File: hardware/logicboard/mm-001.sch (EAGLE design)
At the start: 25 parts, among them IC1 74ALS05N, IC2 LTC485N, IC3 LTC485N

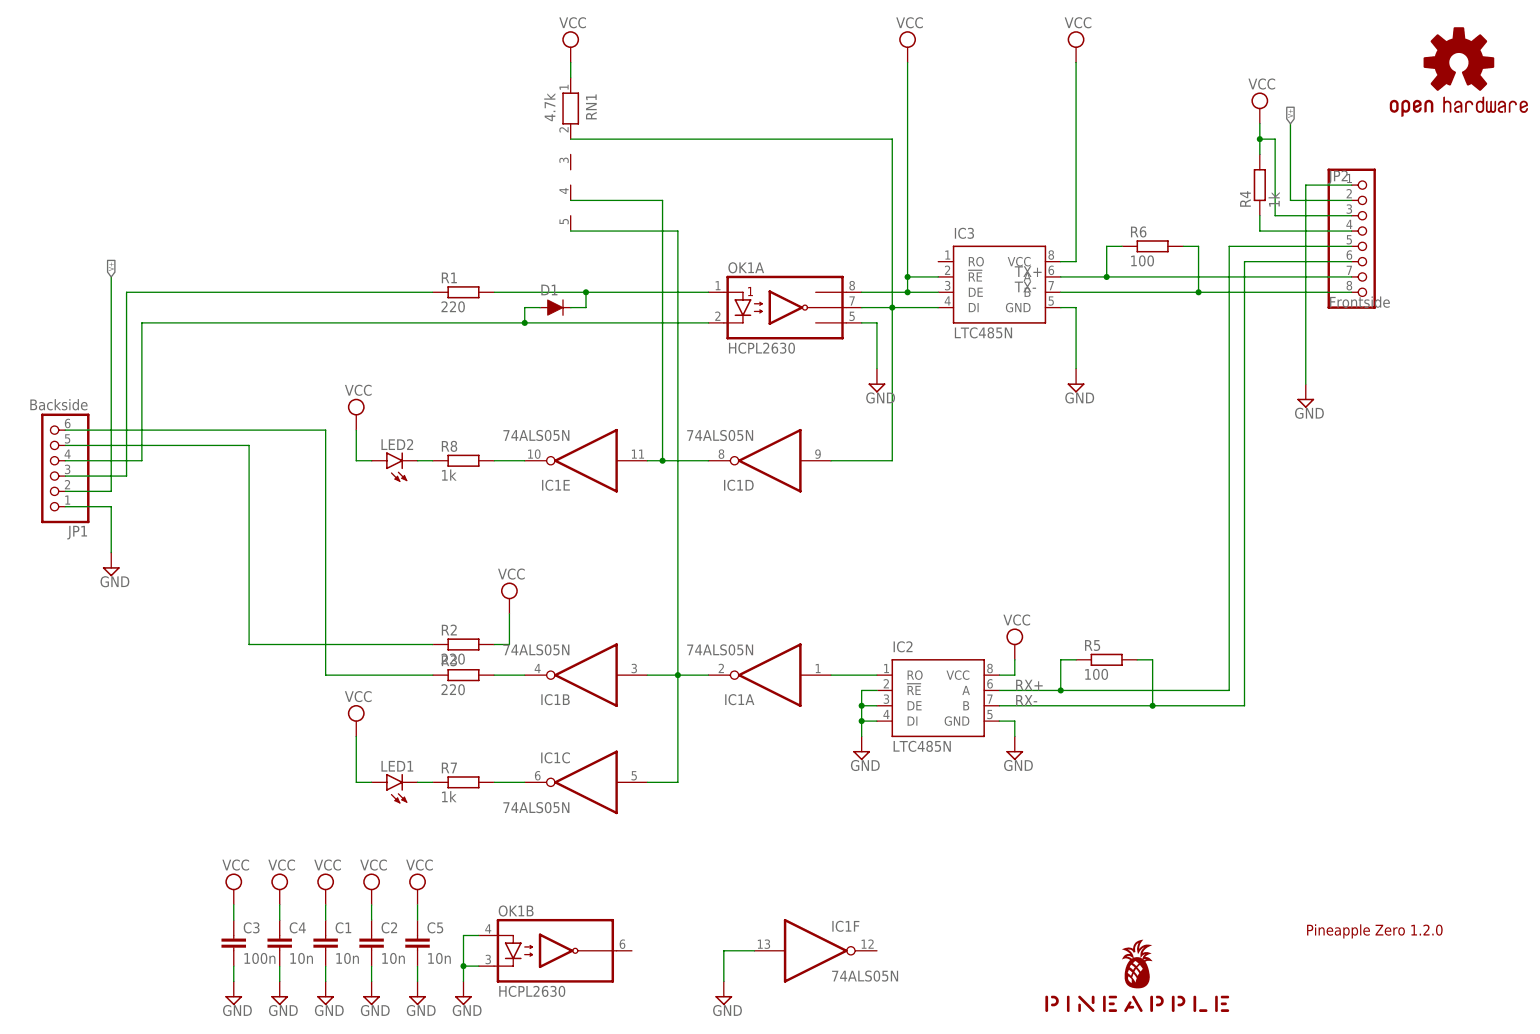
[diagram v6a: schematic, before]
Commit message: TX+/TX-/GND, RX+/RX-/GND.
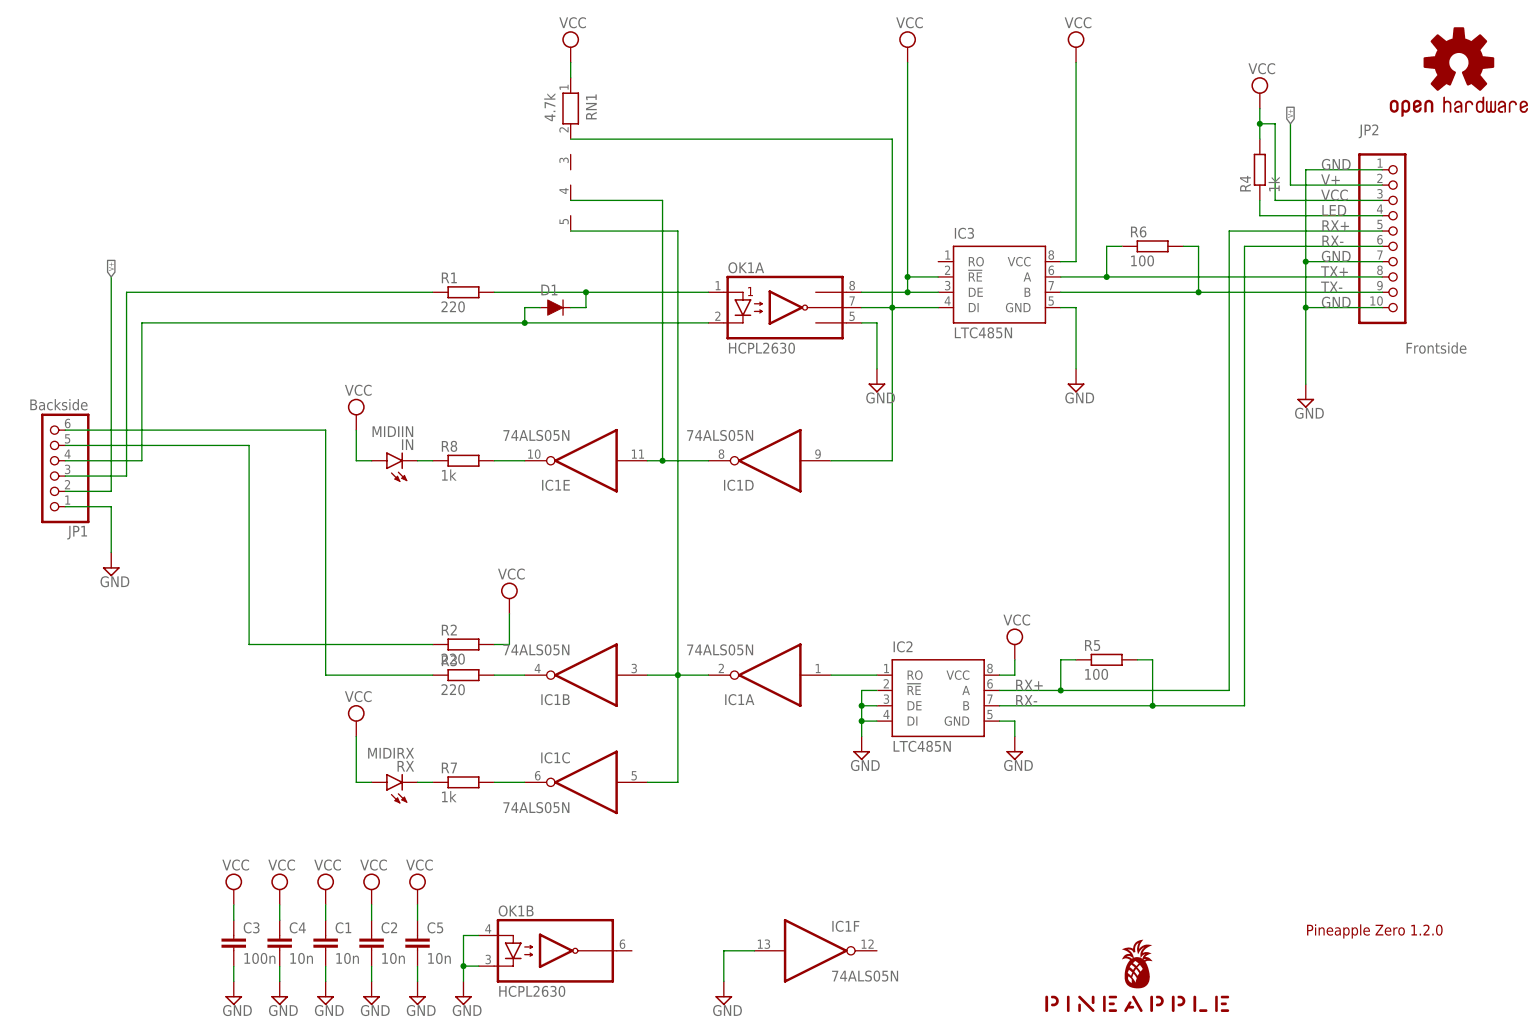
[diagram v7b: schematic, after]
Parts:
- IN: value (none) -> MIDIIN
- JP2: device pinhead:PINHD-1X8 -> pinhead:PINHD-1X10
- RX: value (none) -> MIDIRX
- renumbered LED1 to RX, LED2 to IN
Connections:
- net GND: now also JP2.10, JP2.7
- net TX+: now also JP2.8; no longer JP2.7
- net TX-: now also JP2.9; no longer JP2.8
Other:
- moved on the sheet: R4

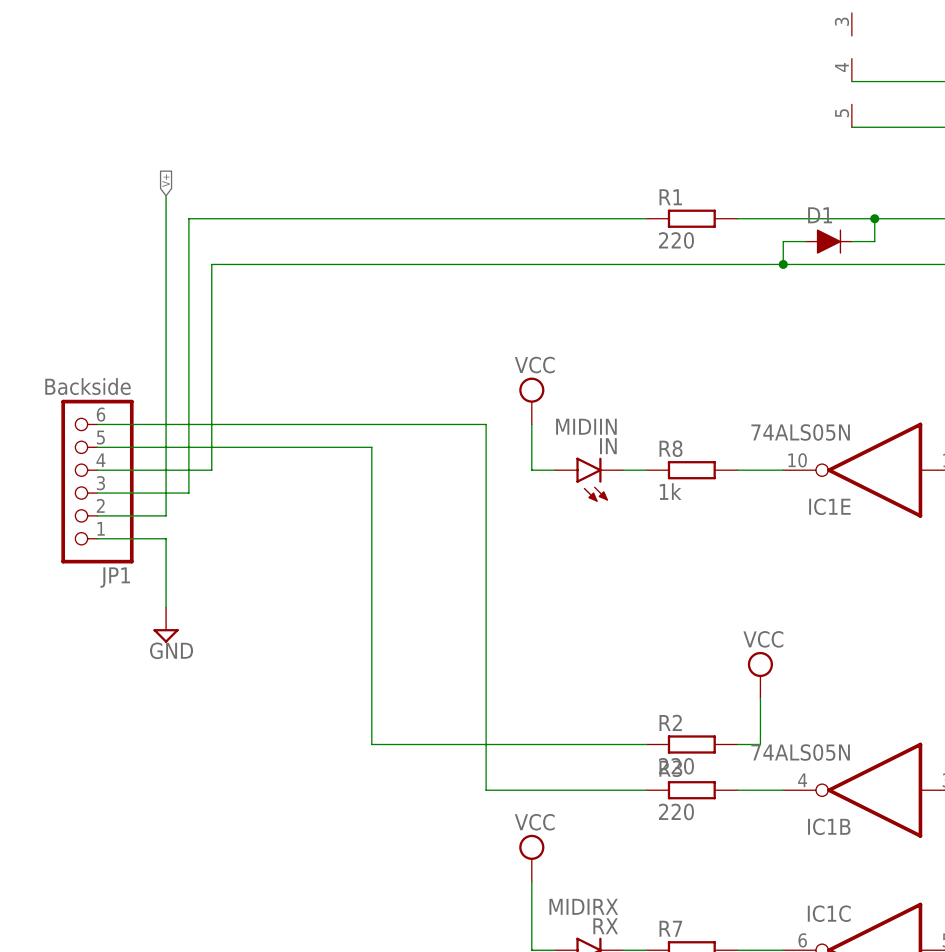
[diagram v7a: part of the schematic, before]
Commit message: Changed positions of the monitor leds.
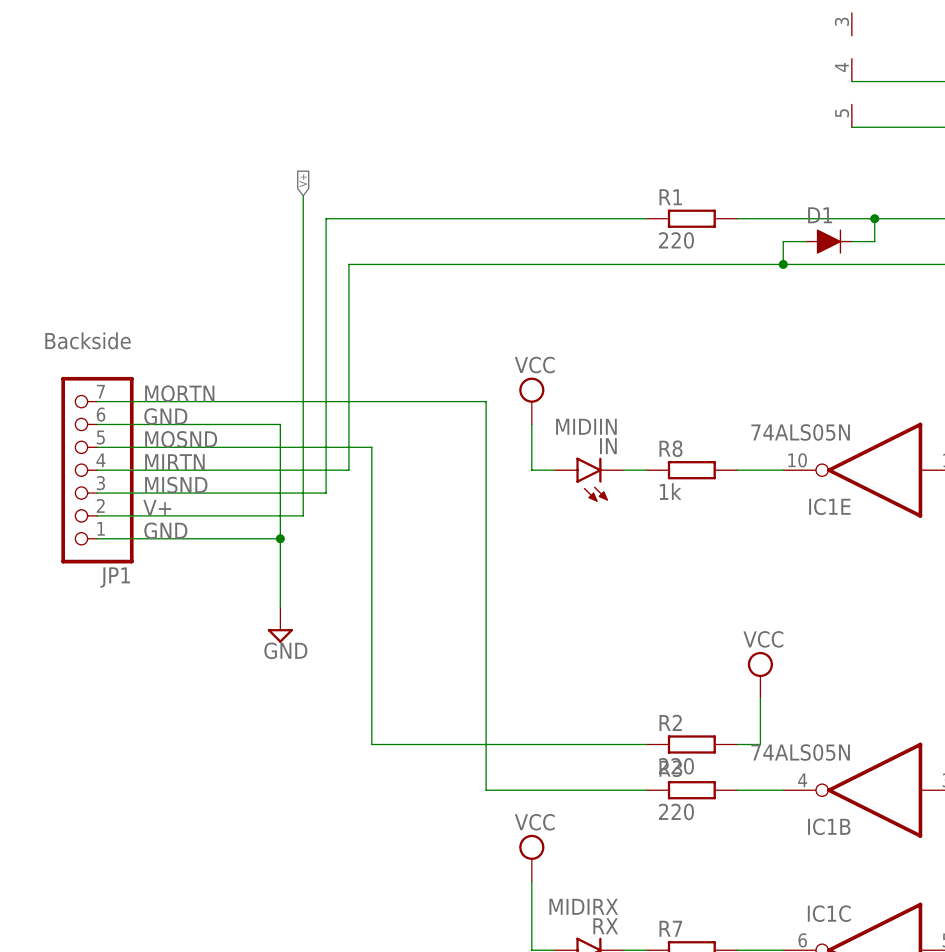
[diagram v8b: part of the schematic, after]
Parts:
- IN, RX: device led:LED3MM -> led:LEDB152
- JP1: device pinhead:PINHD-1X6 -> pinhead:PINHD-1X7
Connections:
- net GND: now also JP1.6
- net MORTN: now also JP1.7; no longer JP1.6
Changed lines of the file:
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@@
 <part name="SUPPLY22" library="supply2" library_urn="urn:adsk.eagle:library:372" deviceset="GND" device=""/>
 <part name="SUPPLY25" library="supply2" library_urn="urn:adsk.eagle:library:372" deviceset="GND" device=""/>
-<part name="JP1" library="pinhead" library_urn="urn:adsk.eagle:library:325" deviceset="PINHD-1X6" device="" package3d_urn="urn:adsk.eagle:package:22472/2" value="Backside"/>
+<part name="JP1" library="pinhead" library_urn="urn:adsk.eagle:library:325" deviceset="PINHD-1X7" device="" package3d_urn="urn:adsk.eagle:package:22477/2" value="Backside"/>
 <part name="JP2" library="pinhead" library_urn="urn:adsk.eagle:library:325" deviceset="PINHD-1X10" device="" package3d_urn="urn:adsk.eagle:package:22406/2" value="Frontside"/>
 <part name="R6" library="rcl" library_urn="urn:adsk.eagle:library:334" deviceset="R-EU_" device="0204/5" package3d_urn="urn:adsk.eagle:package:23488/1" value="100"/>
 <part name="R7" library="rcl" library_urn="urn:adsk.eagle:library:334" deviceset="R-EU_" device="0204/5" package3d_urn="urn:adsk.eagle:package:23488/1" value="1k"/>
-<part name="RX" library="led" library_urn="urn:adsk.eagle:library:259" deviceset="LED" device="3MM" package3d_urn="urn:adsk.eagle:package:15797/1" value="MIDIRX"/>
+<part name="RX" library="led" library_urn="urn:adsk.eagle:library:259" deviceset="LED" device="B152" package3d_urn="urn:adsk.eagle:package:15803/1" value="MIDIRX"/>
 <part name="SUPPLY1" library="supply2" library_urn="urn:adsk.eagle:library:372" deviceset="VCC" device=""/>
 <part name="R8" library="rcl" library_urn="urn:adsk.eagle:library:334" deviceset="R-EU_" device="0204/5" package3d_urn="urn:adsk.eagle:package:23488/1" value="1k"/>
-<part name="IN" library="led" library_urn="urn:adsk.eagle:library:259" deviceset="LED" device="3MM" package3d_urn="urn:adsk.eagle:package:15797/1" value="MIDIIN"/>
+<part name="IN" library="led" library_urn="urn:adsk.eagle:library:259" deviceset="LED" device="B152" package3d_urn="urn:adsk.eagle:package:15803/1" value="MIDIIN"/>
 <part name="SUPPLY6" library="supply2" library_urn="urn:adsk.eagle:library:372" deviceset="VCC" device=""/>
 <part name="SUPPLY19" library="supply2" library_urn="urn:adsk.eagle:library:372" deviceset="GND" device=""/>
@@
 <attribute name="VALUE" x="72.39" y="60.198" size="1.778" layer="96"/>
 </instance>
-<instance part="SUPPLY22" gate="GND" x="17.78" y="81.28" smashed="yes">
-<attribute name="VALUE" x="15.875" y="78.105" size="1.778" layer="96"/>
+<instance part="SUPPLY22" gate="GND" x="30.48" y="81.28" smashed="yes">
+<attribute name="VALUE" x="28.575" y="78.105" size="1.778" layer="96"/>
 </instance>
 <instance part="SUPPLY25" gate="GND" x="215.9" y="109.22" smashed="yes">
@@
 <instance part="JP1" gate="A" x="7.62" y="99.06" smashed="yes" rot="R180">
 <attribute name="NAME" x="13.97" y="88.265" size="1.778" layer="95" rot="R180"/>
-<attribute name="VALUE" x="13.97" y="109.22" size="1.778" layer="96" rot="R180"/>
+<attribute name="VALUE" x="13.97" y="114.3" size="1.778" layer="96" rot="R180"/>
 </instance>
 <instance part="JP2" gate="A" x="231.14" y="137.16" smashed="yes">
@@
 </segment>
 <segment>
-<wire x1="10.16" y1="91.44" x2="17.78" y2="91.44" width="0.1524" layer="91"/>
-<wire x1="17.78" y1="91.44" x2="17.78" y2="83.82" width="0.1524" layer="91"/>
+<wire x1="10.16" y1="91.44" x2="30.48" y2="91.44" width="0.1524" layer="91"/>
+<wire x1="30.48" y1="91.44" x2="30.48" y2="83.82" width="0.1524" layer="91"/>
 <pinref part="SUPPLY22" gate="GND" pin="GND"/>
 <pinref part="JP1" gate="A" pin="1"/>
+<label x="15.24" y="91.44" size="1.778" layer="95"/>
+<pinref part="JP1" gate="A" pin="6"/>
+<wire x1="10.16" y1="104.14" x2="30.48" y2="104.14" width="0.1524" layer="91"/>
+<wire x1="30.48" y1="104.14" x2="30.48" y2="91.44" width="0.1524" layer="91"/>
+<junction x="30.48" y="91.44"/>
+<label x="15.24" y="104.14" size="1.778" layer="95"/>
 </segment>
 <segment>
@@
 <junction x="86.36" y="121.92"/>
 <pinref part="OK1" gate="A" pin="C1"/>
-<wire x1="22.86" y1="121.92" x2="86.36" y2="121.92" width="0.1524" layer="91"/>
-<wire x1="22.86" y1="121.92" x2="22.86" y2="99.06" width="0.1524" layer="91"/>
-<wire x1="10.16" y1="99.06" x2="22.86" y2="99.06" width="0.1524" layer="91"/>
+<wire x1="38.1" y1="121.92" x2="86.36" y2="121.92" width="0.1524" layer="91"/>
+<wire x1="38.1" y1="121.92" x2="38.1" y2="99.06" width="0.1524" layer="91"/>
+<wire x1="10.16" y1="99.06" x2="38.1" y2="99.06" width="0.1524" layer="91"/>
 <pinref part="JP1" gate="A" pin="4"/>
+<label x="15.24" y="99.06" size="1.778" layer="95"/>
 </segment>
 </net>
@@
 <wire x1="71.12" y1="63.5" x2="53.34" y2="63.5" width="0.1524" layer="91"/>
 <pinref part="R3" gate="G$1" pin="1"/>
-<pinref part="JP1" gate="A" pin="6"/>
-<wire x1="53.34" y1="104.14" x2="53.34" y2="63.5" width="0.1524" layer="91"/>
-<wire x1="10.16" y1="104.14" x2="53.34" y2="104.14" width="0.1524" layer="91"/>
+<wire x1="53.34" y1="106.68" x2="53.34" y2="63.5" width="0.1524" layer="91"/>
+<label x="15.24" y="106.68" size="1.778" layer="95"/>
+<pinref part="JP1" gate="A" pin="7"/>
+<wire x1="10.16" y1="106.68" x2="53.34" y2="106.68" width="0.1524" layer="91"/>
 </segment>
 </net>
@@
 <segment>
 <pinref part="R1" gate="G$1" pin="1"/>
-<wire x1="71.12" y1="127" x2="20.32" y2="127" width="0.1524" layer="91"/>
-<wire x1="10.16" y1="96.52" x2="20.32" y2="96.52" width="0.1524" layer="91"/>
-<wire x1="20.32" y1="96.52" x2="20.32" y2="127" width="0.1524" layer="91"/>
+<wire x1="71.12" y1="127" x2="35.56" y2="127" width="0.1524" layer="91"/>
+<wire x1="10.16" y1="96.52" x2="35.56" y2="96.52" width="0.1524" layer="91"/>
+<wire x1="35.56" y1="96.52" x2="35.56" y2="127" width="0.1524" layer="91"/>
 <pinref part="JP1" gate="A" pin="3"/>
+<label x="15.24" y="96.52" size="1.778" layer="95"/>
 </segment>
 </net>
@@
 <wire x1="40.64" y1="101.6" x2="40.64" y2="68.58" width="0.1524" layer="91"/>
 <wire x1="10.16" y1="101.6" x2="40.64" y2="101.6" width="0.1524" layer="91"/>
+<label x="15.24" y="101.6" size="1.778" layer="95"/>
 </segment>
 </net>
@@
 </segment>
 <segment>
-<wire x1="10.16" y1="93.98" x2="17.78" y2="93.98" width="0.1524" layer="91"/>
-<wire x1="17.78" y1="93.98" x2="17.78" y2="129.54" width="0.1524" layer="91"/>
+<wire x1="10.16" y1="93.98" x2="33.02" y2="93.98" width="0.1524" layer="91"/>
+<wire x1="33.02" y1="93.98" x2="33.02" y2="129.54" width="0.1524" layer="91"/>
 <pinref part="JP1" gate="A" pin="2"/>
-<label x="17.78" y="129.54" size="0.8128" layer="95" rot="R90" xref="yes"/>
-</segment>
-</net>
+<label x="33.02" y="129.54" size="0.8128" layer="95" rot="R90" xref="yes"/>
+<label x="15.24" y="93.98" size="1.778" layer="95"/>
+</segment>
+</net>
